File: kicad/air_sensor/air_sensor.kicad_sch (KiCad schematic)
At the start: 16 parts, among them J1 Barrel_Jack, U1 ATmega328-A, U2 AMS1117CD-5.0, U3 AMS1117-3.3

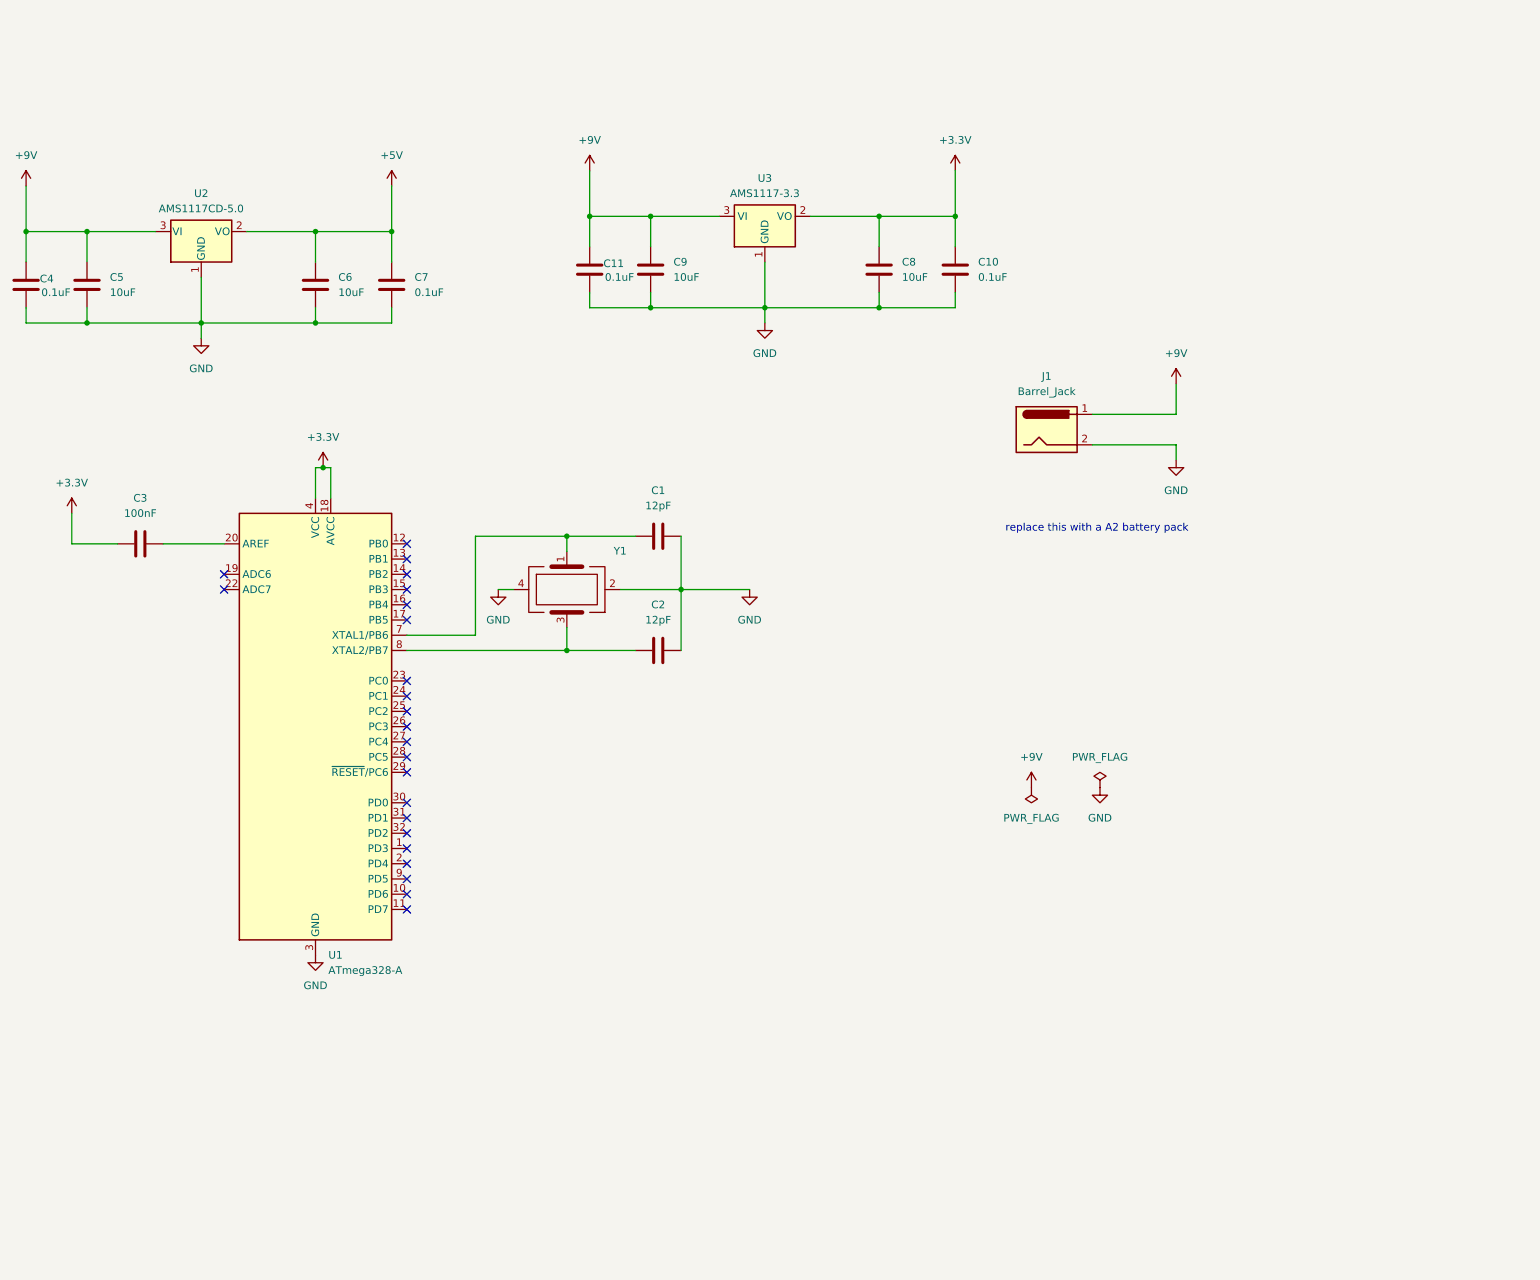
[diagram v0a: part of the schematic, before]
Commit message: updated schema
added 5V 3A buck converter
refined 3v3 LDO
added symbols for new components
added text comments for designing the pcb
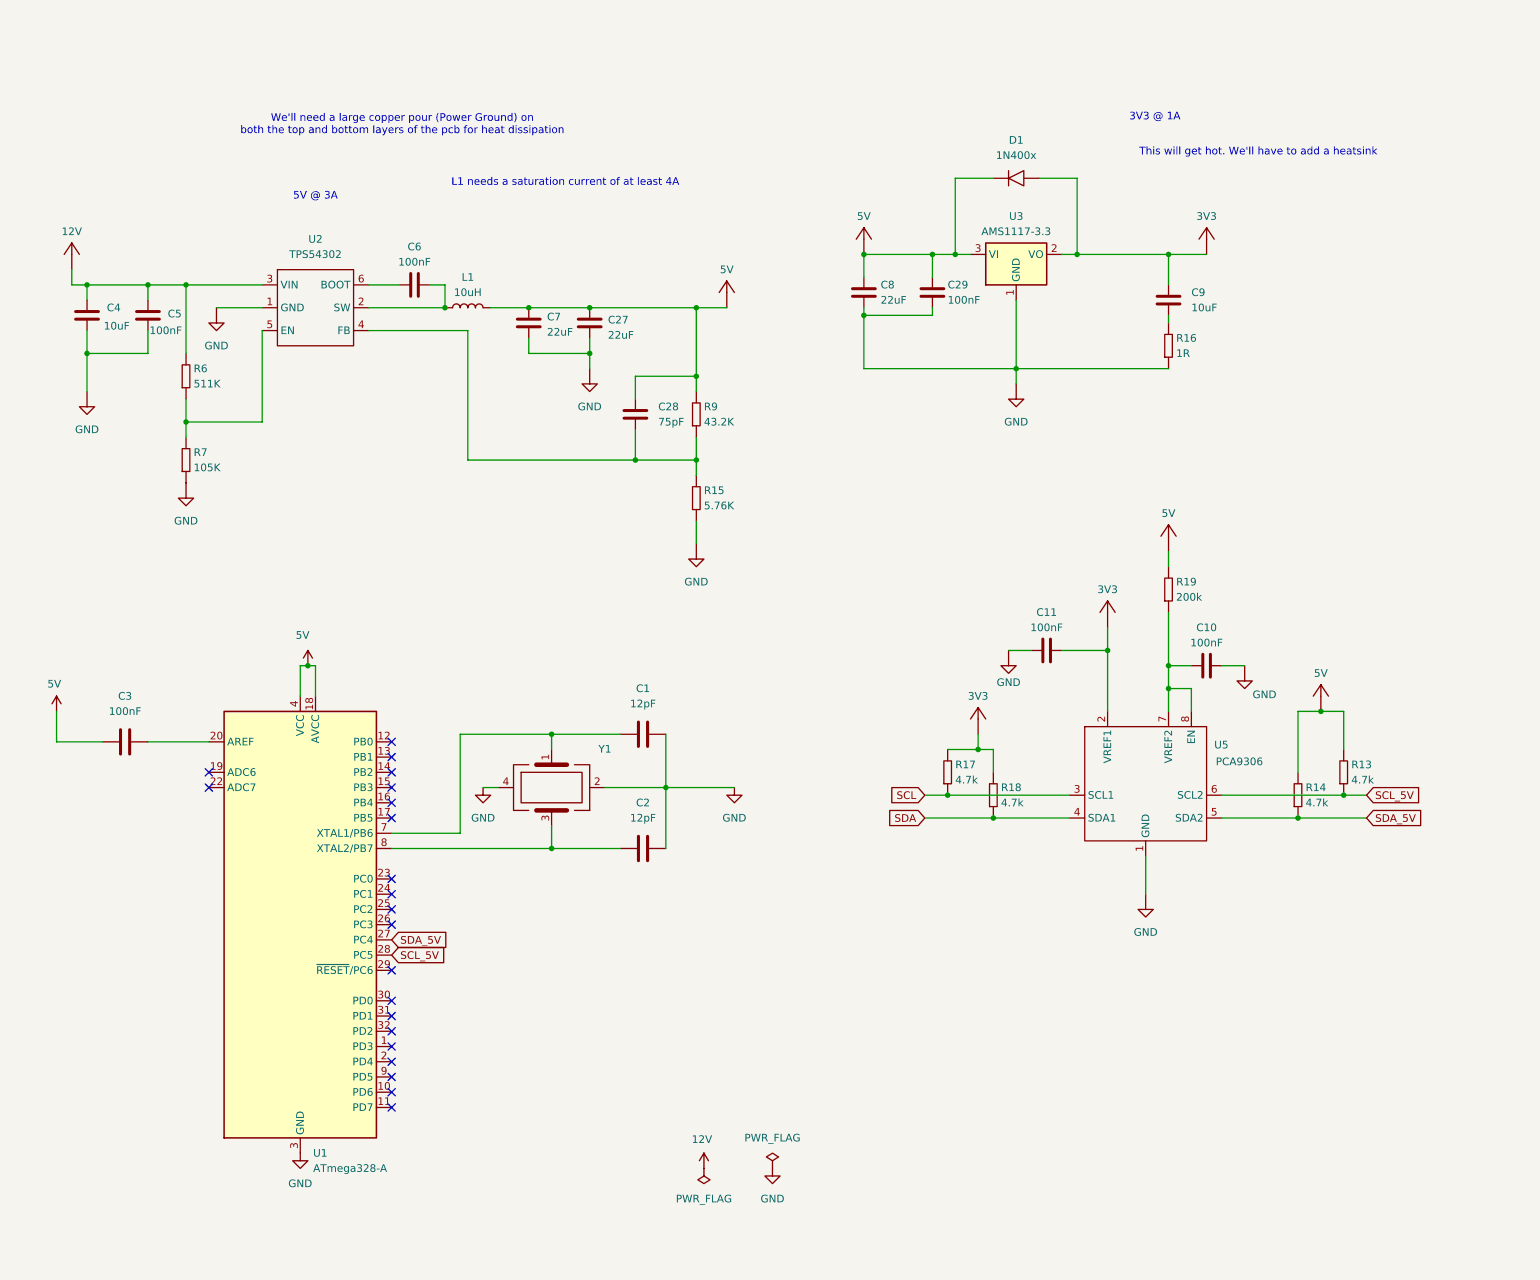
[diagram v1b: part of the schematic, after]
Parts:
- removed C10, C11, C4, C7: 0.1uF, symbol Device:C
- removed C5, C6, C8, C9: 10uF, symbol Device:C
- removed J1: Barrel_Jack, symbol Connector:Barrel_Jack
- removed U2: AMS1117CD-5.0, Package_TO_SOT_SMD:TO-252-3_TabPin2, symbol Regulator_Linear:AMS1117CD-5.0
- added C10, C11, C29, C5, C6: 100nF, symbol common:Capacitor
- added C27, C7, C8: 22uF, symbol common:Capacitor
- added C28: 75pF, symbol common:Capacitor
- added C4, C9: 10uF, symbol common:Capacitor
- added D1: 1N400x, symbol common:Diode
- added L1: 10uH, symbol common:Inductor
- added R13, R14, R17, R18: 4.7k, symbol common:Resistor
- added R15: 5.76K, symbol common:Resistor
- added R16: 1R, symbol common:Resistor
- added R19: 200k, symbol common:Resistor
- added R6: 511K, symbol common:Resistor
- added R7: 105K, symbol common:Resistor
- added R9: 43.2K, symbol common:Resistor
- added U2: TPS54302, symbol air_sens_lib:TPS54302
- added U5: PCA9306, symbol air_sens_lib:PCA9306
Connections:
- net +9V is gone; now on net 5V: U3.3 (VI)
- net GND: now also C10.2, C11.1, C27.1, C29.1, C4.1, C5.1, C7.2, C8.1, R15.1, R16.1, R7.1, U2.1 (GND), U5.1 (GND)
- net SDA_5V: now reaches U1.27 (PC4)
- net SDA_5V: now also R14.1, U5.5 (SDA2)
- net SCL_5V: now reaches U1.28 (PC5)
- net SCL_5V: now also R13.1, U5.6 (SCL2)
- net +3.3V renamed 5V
- net 5V: now also C27.2, C28.2, C29.2, C7.1, C8.2, D1., L1.2, R13.2, R14.2, R19.2, R9.2; no longer U3.2 (VO)
- new net: C10.1, R19.1, U5.7 (VREF2), U5.8 (EN)
- new net: C28.1, R15.2, R9.1, U2.4 (FB)
- new net: C6.2, L1.1, U2.2 (SW)
- new net: R6.1, R7.2, U2.5 (EN)
- new net: C9.1, R16.2
- new net: C6.1, U2.6 (BOOT)
- new net 12V: C4.2, C5.2, R6.2, U2.3 (VIN)
- new net 3V3: C11.2, C9.2, D1., R17.2, R18.2, U3.2 (VO), U5.2 (VREF1)
- new net SCL: R17.1, U5.3 (SCL1)
- new net SDA: R18.1, U5.4 (SDA1)
- no-connect marks 23 -> 21
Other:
- note added: "3V3 @ 1A"
- note added: "5V @ 3A"
- note added: "L1 needs a saturation current of at least 4A"
- note added: "This will get hot. We'll have to add a heatsink"
- note added: "We'll need a large copper pour (Power Ground) on both the top and bottom layers of the pcb for heat dissipation"
- note removed: "replace this with a A2 battery pack"
- moved on the sheet: C1, C2, C3, U1, U3, Y1

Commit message: updated power symbol labels, replaced power symbols in schematic with our own custom symbols
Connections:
- net 3V3: now also D1.2 (A); no longer D1.
- net 5V: now also D1.1 (K); no longer D1.

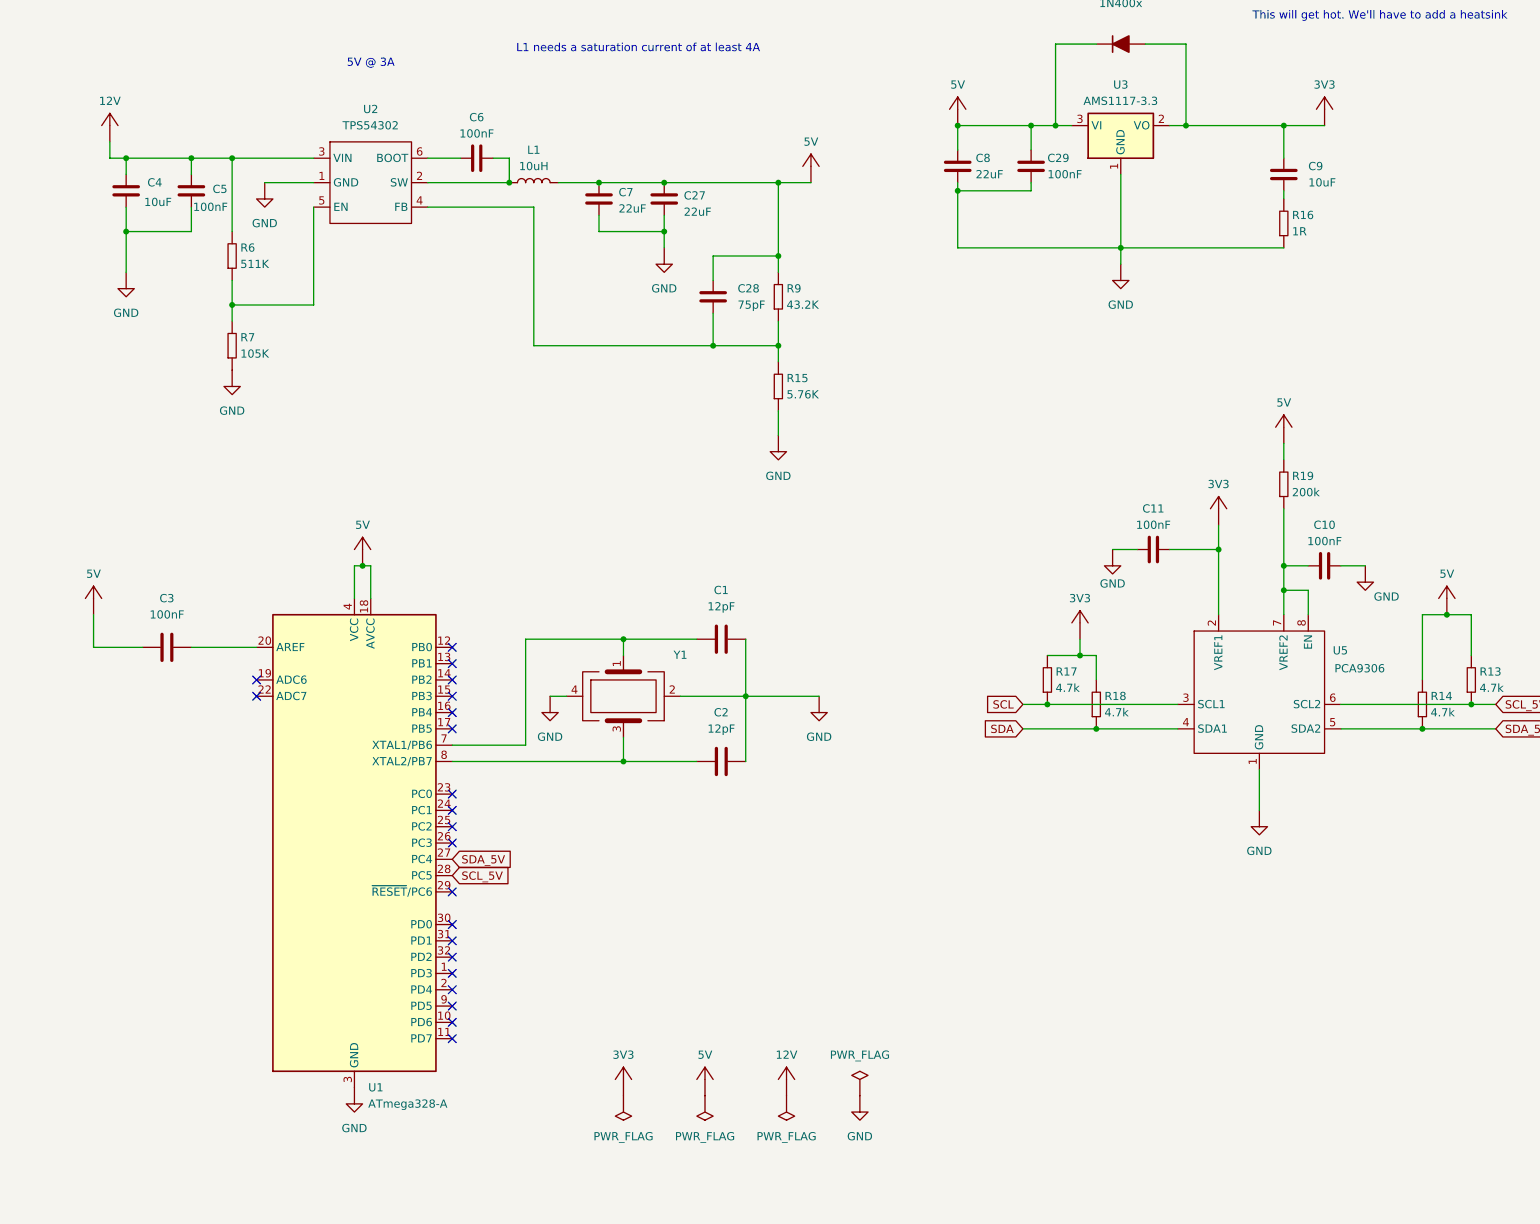
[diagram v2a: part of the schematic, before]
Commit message: added pcb for gas and climate modules
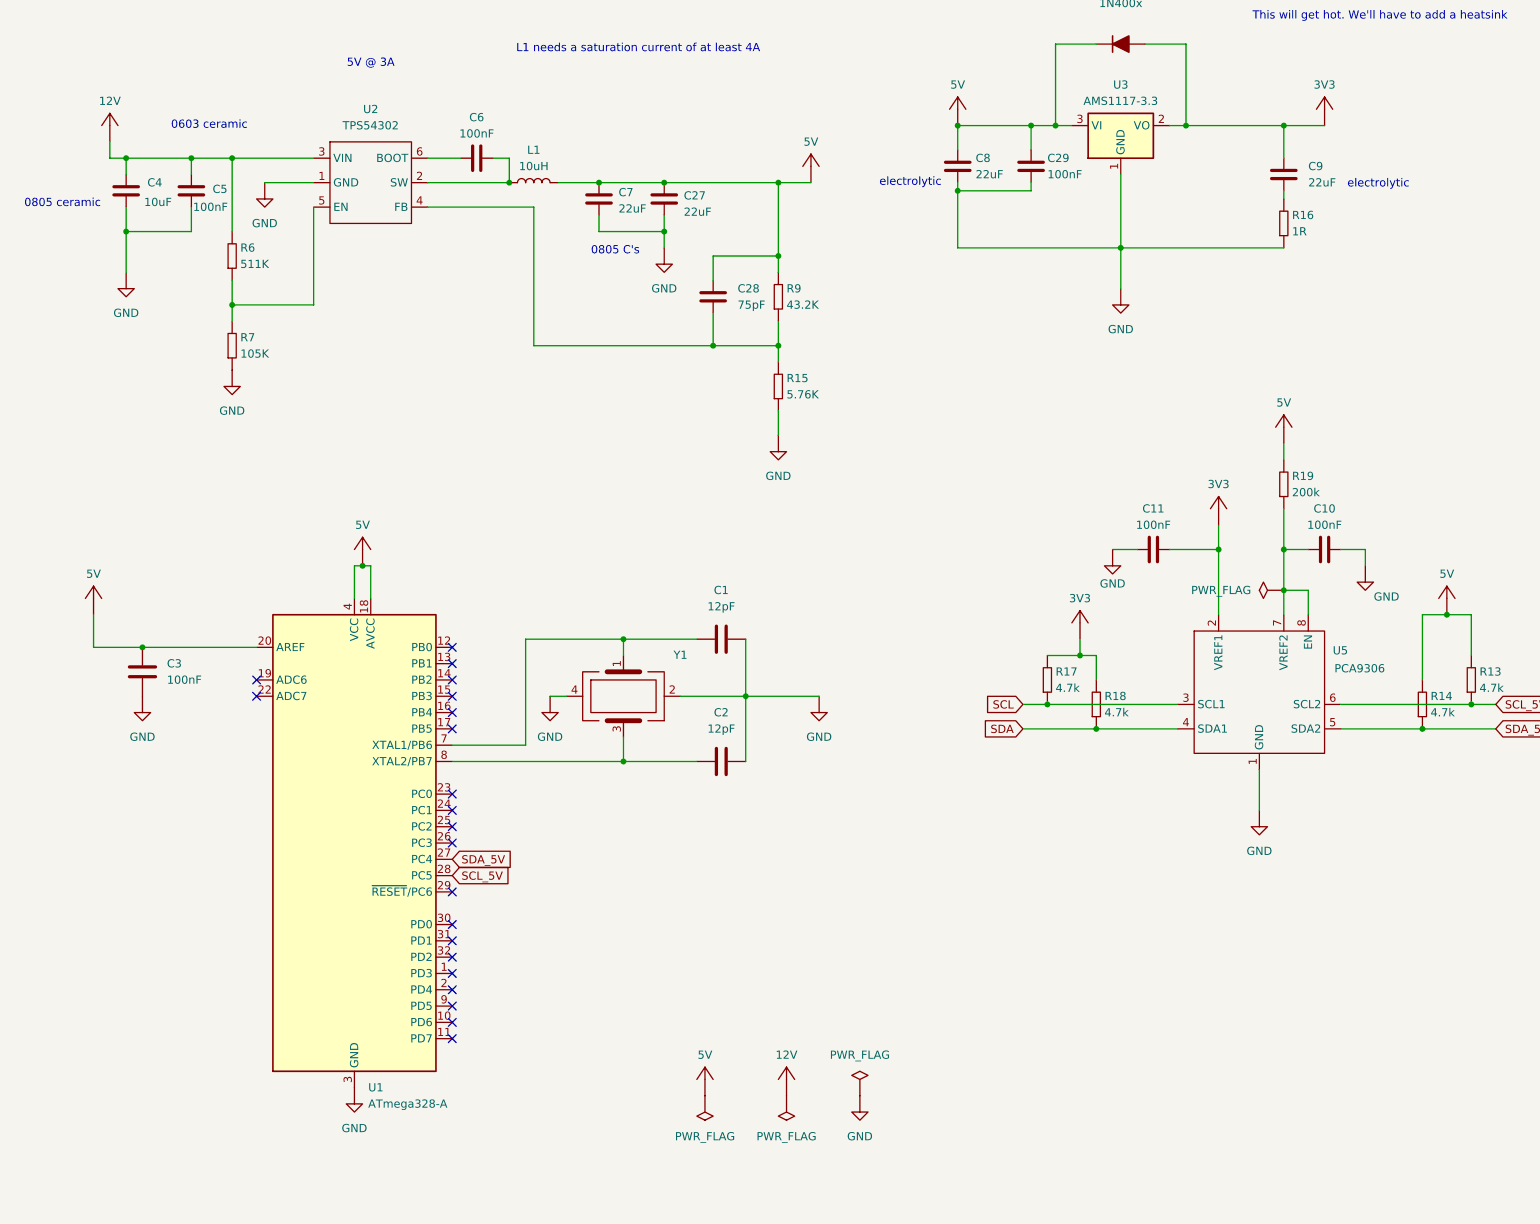
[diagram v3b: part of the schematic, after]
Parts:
- C1, C10, C11, C2, C28, C29, C3, C5, C6: footprint (none) -> common:C_0603
- C27, C4, C7: footprint (none) -> common:C_0805
- C8: footprint (none) -> common:C_Elec_SMD_5x5.4
- C9: value 10uF -> 22uF; footprint (none) -> common:C_Elec_SMD_5x5.4
- D1: footprint (none) -> common:D_SOD123
- L1: footprint (none) -> common:L_CHILISIN_5.5X5.2
- R13, R14, R15, R16, R17, R18, R19, R6, R7, R9: footprint (none) -> common:R_0603
- U2: footprint (none) -> air_sens_foots:TPS54302
- U5: footprint (none) -> air_sens_foots:PCA9306
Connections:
- net 5V: now also C3.1, U1.20 (AREF); no longer C3.2
- net GND: now also C3.2
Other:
- note added: "0603 ceramic"
- note added: "0805 C's"
- note added: "0805 ceramic"
- note added: "electrolytic"
- moved on the sheet: C10, C3
